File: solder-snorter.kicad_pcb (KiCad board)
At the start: 2 copper layers, 80 x 33.5 mm, 17 parts, among them J1 USB_B_Micro, M1 Fan, SW1 SW_SPDT, U1 MCP73831, U2 TLV61046A

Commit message: Finished first cut at layout
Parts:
- SW1: moved to F.Cu
- moved REF** 114.0 mm to (137.2, 151.2), turned to 90 degrees
- moved L1 75.1 mm to (154.2, 127.2), turned to 0 degrees
- moved U2 71.8 mm to (154.2, 122.2), turned to 180 degrees
- moved SW1 70.7 mm to (163.9, 131.2), turned to 90 degrees
- moved C3 64.0 mm to (148.8, 122.5), turned to 90 degrees
- moved C4 62.2 mm to (152.8, 118.2), turned to 0 degrees
- moved J1 62.1 mm to (162.4, 115.5), turned to 90 degrees
- moved BT1 61.0 mm to (155.5, 118.5), turned to 270 degrees
- moved REF** 58.4 mm to (137.2, 79.8), turned to 90 degrees
- moved M1 47.3 mm to (146.0, 77.5), turned to 90 degrees
- moved C1 37.2 mm to (154.2, 107.9)
- moved D1 36.1 mm to (160.2, 105.8), turned to 270 degrees
- moved D2 35.5 mm to (162.5, 105.8), turned to 90 degrees
- moved R2 33.8 mm to (157.6, 106.2), turned to 270 degrees
- moved U1 33.2 mm to (154.2, 103.8), turned to 270 degrees
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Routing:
- net VBAT: track 0.00 -> 55.6 mm, vias 0 -> 24
- net +12V: track 0.00 -> 54.0 mm, vias 0 -> 1
- net VBATSW: track 0.00 -> 25.5 mm
- net Net-(C1-Pad1): track 0.00 -> 11.5 mm, vias 0 -> 41
- net Net-(D1-Pad1): track 0.00 -> 4.92 mm
- net GND: track 0.00 -> 2.71 mm, vias 0 -> 41
- net Net-(R2-Pad1): track 0.00 -> 2.63 mm
- net Net-(R1-Pad1): track 0.00 -> 2.59 mm
- added copper zone on B.Cu, net GND
- added copper zone on F.Cu, net GND
- added copper zone on B.Cu, net Net-(C1-Pad1)
- added copper zone on F.Cu, net Net-(C1-Pad1)
- added copper zone on F.Cu, net Net-(L1-Pad2)
- added copper zone on B.Cu, net VBAT
- added copper zone on F.Cu, net VBAT
- added copper zone on F.Cu, net VBATSW
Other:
- board size 80 x 33.5 mm -> 33.5 x 80 mm
- net class Default: clearance 0.2 -> 0.25
- net class Min added: clearance 0.1, trace_width 0.1, via_dia 0.45, via_drill 0.2
- rule pad_to_mask_clearance: 0.05 -> 0
- rule trace_clearance: 0.2 -> 0.25
- rule trace_min: 0.2 -> 0.1
- rule via_min_drill: 0.3 -> 0.2
- rule via_min_size: 0.4 -> 0.45

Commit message: Finished v1.0 layout
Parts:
- removed REF** (x2): MountingHole_4.3mm_M4_DIN965, MountingHole:MountingHole_4.3mm_M4_DIN965
- added J2: Conn_01x01, MountingHole:MountingHole_4.3mm_M4_DIN965, F.Cu at (137.2, 79.8)
- added J3: Conn_01x01, MountingHole:MountingHole_4.3mm_M4_DIN965, F.Cu at (137.2, 151.2)
- added TP1: GND, TestPoint:TestPoint_Pad_2.0x2.0mm, F.Cu at (163.8, 100.5)
- added TP2: VBUS, TestPoint:TestPoint_Pad_2.0x2.0mm, F.Cu at (161.0, 122.0)
- added TP3: SW, TestPoint:TestPoint_Pad_2.0x2.0mm, F.Cu at (159.5, 126.0)
- added TP4: VBAT, TestPoint:TestPoint_Pad_2.0x2.0mm, F.Cu at (163.7, 94.5)
- added TP5: +12V, TestPoint:TestPoint_Pad_2.0x2.0mm, F.Cu at (145.5, 83.5)
- moved SW1 4.80 mm to (163.9, 136.0)
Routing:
- net Net-(L1-Pad2): track 0.00 -> 5.59 mm
- net +12V: track 54.0 -> 58.6 mm, vias 1 -> 2
- net VBAT: track 55.6 -> 59.5 mm, vias 24 -> 23
- net Net-(C1-Pad1): track 11.5 -> 14.0 mm
- net GND: track 2.71 -> 4.49 mm, vias 41 -> 53
- net VBATSW: track 25.5 -> 26.5 mm
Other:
- board text added: "+12V"
- board text added: "GND"
- board text added: "OFF"
- board text added: "ON"
- board text added: "SW"
- board text added: "Solder Snorter v1.0"
- board text added: "VBAT"
- board text added: "VBUS"

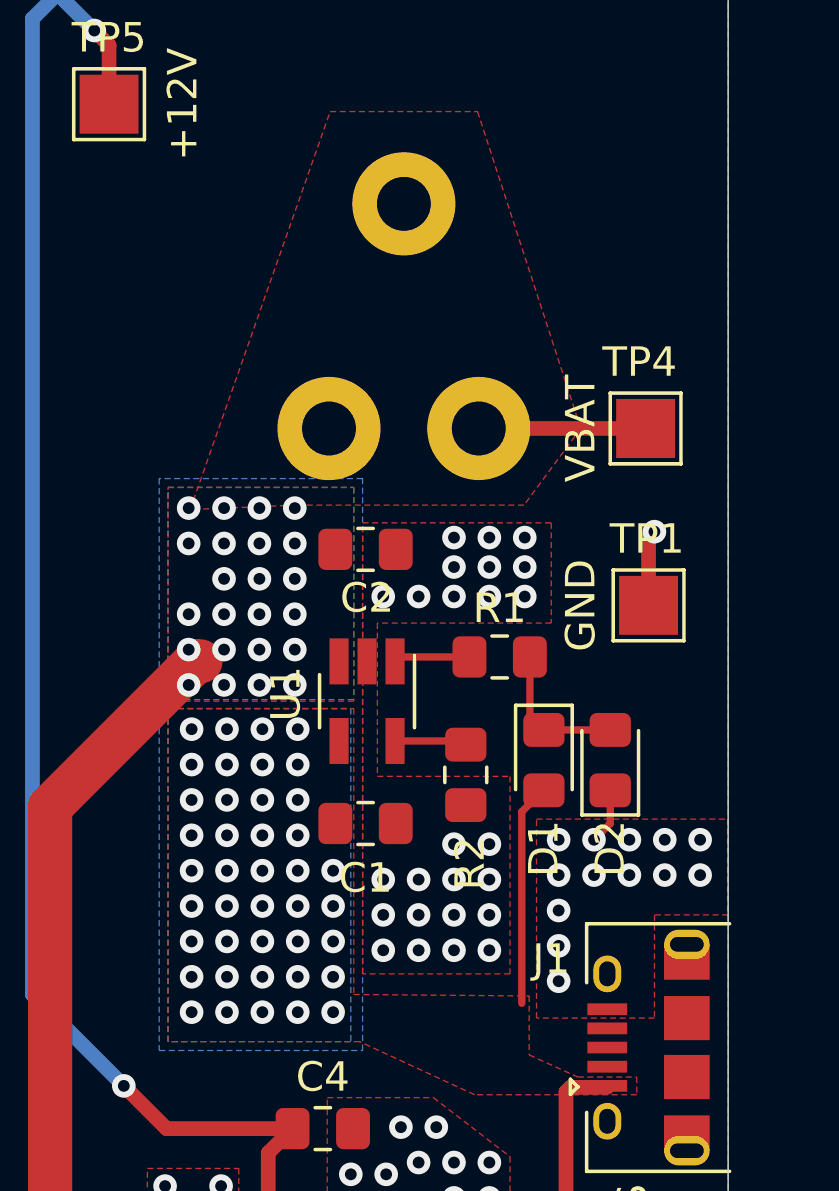
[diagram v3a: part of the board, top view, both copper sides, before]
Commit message: Fix LED resistor mistake
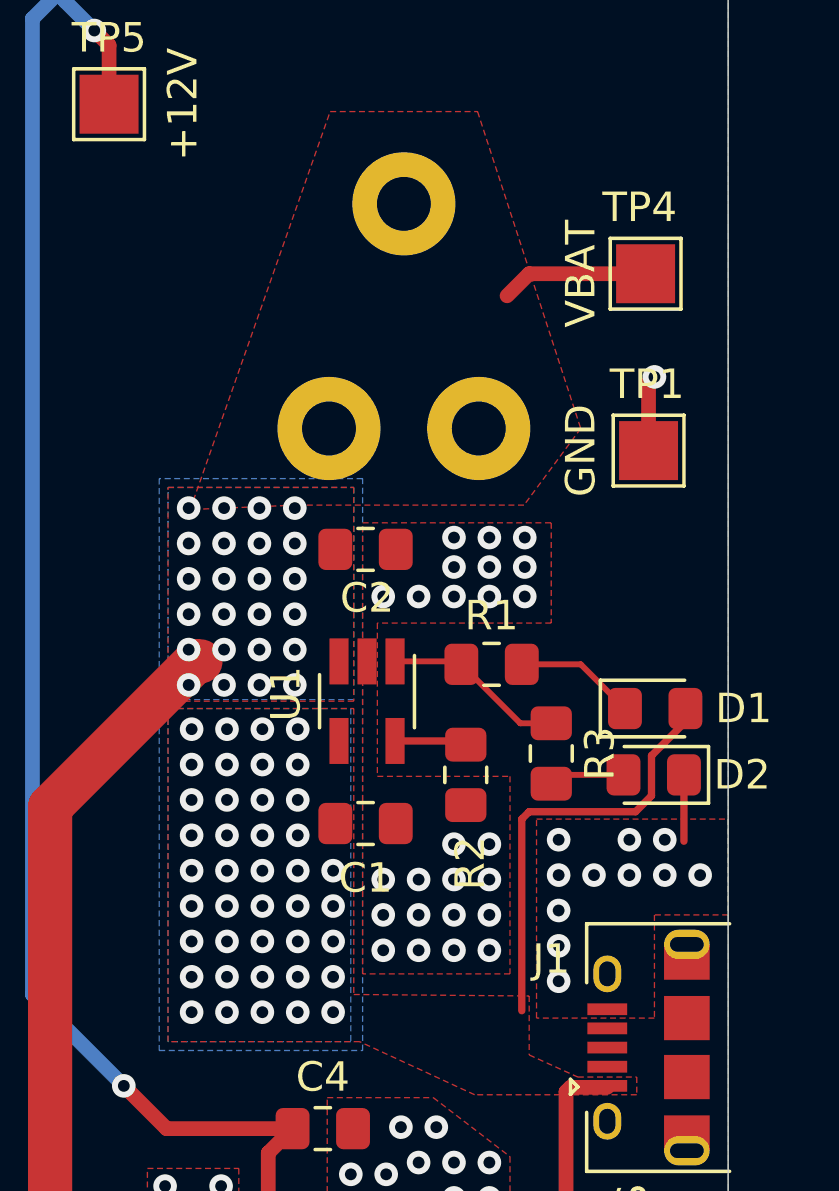
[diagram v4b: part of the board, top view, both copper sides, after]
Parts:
- removed J2, J3: Conn_01x01, MountingHole:MountingHole_4.3mm_M4_DIN965
- added H1: MountingHole, MountingHole:MountingHole_4.3mm_M4_DIN965, F.Cu at (137.2, 79.8)
- added H2: MountingHole, MountingHole:MountingHole_4.3mm_M4_DIN965, F.Cu at (137.2, 151.2)
- added R3: 470, Resistor_SMD:R_0805_2012Metric_Pad1.15x1.40mm_HandSolder, F.Cu at (160.5, 105.5)
- moved TP1 5.25 mm to (163.8, 95.2)
- moved TP4 5.25 mm to (163.7, 89.2)
- moved D1 4.16 mm to (164.0, 104.0), turned to 0 degrees
- moved D2 1.56 mm to (164.0, 106.2), turned to 180 degrees
- moved R1 0.37 mm to (158.5, 102.5)
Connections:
- D2 pad 2: Net-(D1-Pad1) -> Net-(D2-Pad2)
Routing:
- net Net-(C1-Pad1): track 14.0 -> 21.1 mm
- net Net-(R1-Pad1): track 2.59 -> 6.17 mm
- net Net-(D2-Pad2): track 0.00 -> 2.57 mm
- net Net-(D1-Pad1): track 4.92 -> 4.12 mm
- net VBAT: track 59.5 -> 58.9 mm, vias 23 -> 24
- net GND: track 4.49 -> 4.83 mm, vias 53 -> 51
